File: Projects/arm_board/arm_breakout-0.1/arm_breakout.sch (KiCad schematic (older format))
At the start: 4 parts, among them P1 CONN_3X2, U1 2534-6002UB_34-pin_header, U2 Teensy3.1, U3 MCP2561

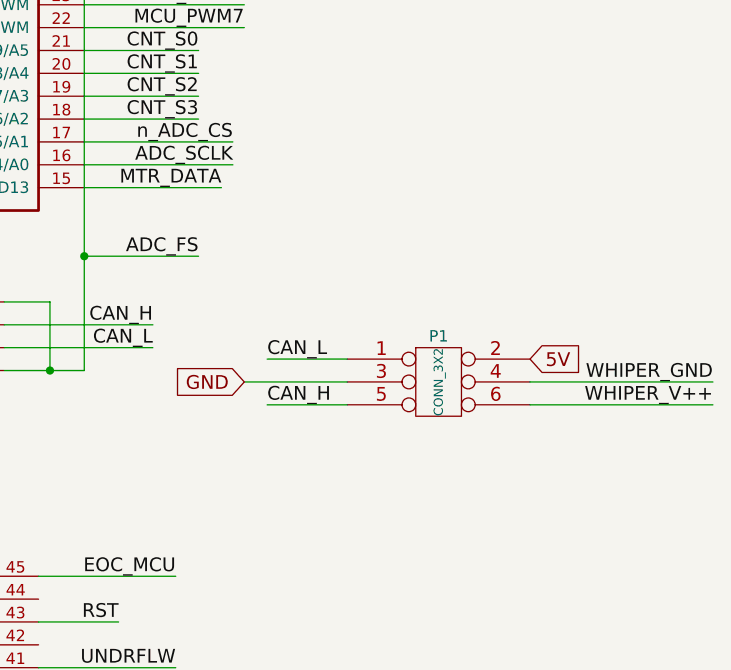
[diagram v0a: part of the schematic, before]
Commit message: Arm Breakout: Finish schematic, assign footprints
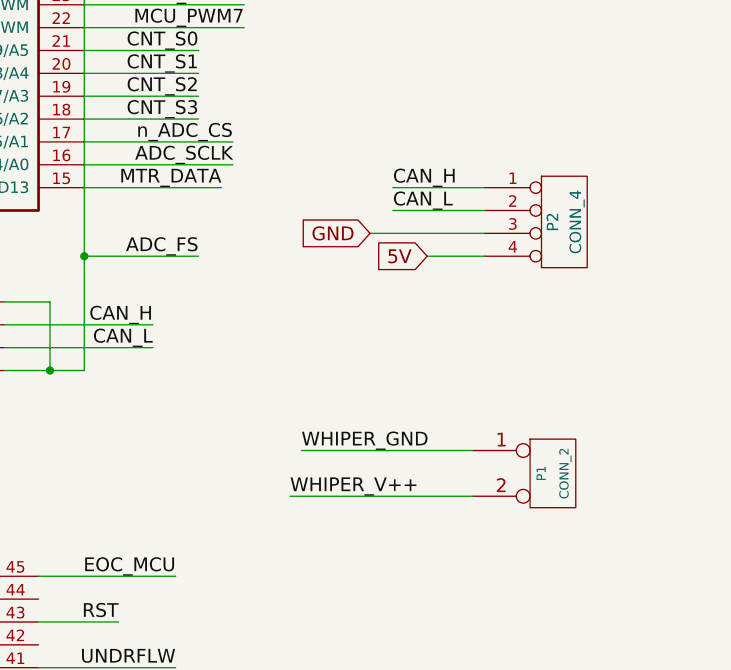
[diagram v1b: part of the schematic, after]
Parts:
- removed P1: CONN_3X2, symbol CONN_3X2
- added P1: CONN_2, ArmFootprints:2-pin-connector, symbol CONN_2
- added P2: CONN_4, ArmFootprints:4-pin_connector, symbol CONN_4
- U1: footprint (none) -> ArmFootprints:34-pin_2534-6002UB
- U2: footprint (none) -> ArmFootprints:Teensy3.1
- U3: footprint (none) -> ArmFootprints:MCP2562
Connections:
- net 5V: now also P2.4 (P4)
- net CAN_H: now also P2.1 (P1)
- net CAN_L: now also P2.2 (P2)
- net GND: now also P2.3 (P3)
- net WHIPER_GND: now also P1.1 (P1)
- net WHIPER_V++: now also P1.2 (PM)
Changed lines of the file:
@@
 F 0 "U3" H 4950 4500 60  0000 L CNN
 F 1 "MCP2561" H 4950 4400 60  0000 L CNN
-F 2 "" H 4750 4250 60  0000 C CNN
+F 2 "ArmFootprints:MCP2562" H 4750 4250 60  0001 C CNN
 F 3 "" H 4750 4250 60  0000 C CNN
 	1    5300 4150
@@
 F 0 "U1" H 2100 2200 60  0000 C CNN
 F 1 "2534-6002UB_34-pin_header" V 2100 3100 60  0000 C CNN
-F 2 "" H 2100 3250 60  0000 C CNN
+F 2 "ArmFootprints:34-pin_2534-6002UB" H 2100 3250 60  0001 C CNN
 F 3 "" H 2100 3250 60  0000 C CNN
 	1    2100 3250
@@
 F 0 "U2" H 4600 2500 60  0000 L CNN
 F 1 "Teensy3.1" H 4600 2400 60  0000 L CNN
-F 2 "" H 4400 2250 60  0000 C CNN
+F 2 "ArmFootprints:Teensy3.1" H 4400 2250 60  0001 C CNN
 F 3 "" H 4400 2250 60  0000 C CNN
 	3    4400 2250
@@
 F 0 "U2" H 4800 5200 60  0000 L CNN
 F 1 "Teensy3.1" H 4800 5100 60  0000 L CNN
-F 2 "" H 4600 4950 60  0000 C CNN
+F 2 "ArmFootprints:Teensy3.1" H 4600 4950 60  0001 C CNN
 F 3 "" H 4600 4950 60  0000 C CNN
 	2    4600 4950
@@
 Text GLabel 3900 2250 0    60   Input ~ 0
 GND
-$Comp
-L CONN_3X2 P1
-U 1 1 57225D6F
-P 7750 4450
-F 0 "P1" H 7750 4700 50  0000 C CNN
-F 1 "CONN_3X2" V 7750 4500 40  0000 C CNN
-F 2 "" H 7750 4450 60  0000 C CNN
-F 3 "" H 7750 4450 60  0000 C CNN
-	1    7750 4450
-	1    0    0    -1
-$EndComp
-Text GLabel 8150 4300 2    60   Input ~ 0
-5V
-Text GLabel 6900 4400 0    60   Input ~ 0
-GND
-Text Label 8950 4400 2    60   ~ 0
+Text Label 7150 4700 0    60   ~ 0
 WHIPER_GND
-Text Label 8950 4500 2    60   ~ 0
+Text Label 7100 4900 0    60   ~ 0
 WHIPER_V++
-Text Label 7000 4500 0    60   ~ 0
-CAN_H
 Wire Wire Line
 	1300 2550 1800 2550
@@
 Wire Wire Line
 	6200 4350 5850 4350
-Wire Wire Line
-	8950 4400 8150 4400
-Wire Wire Line
-	8950 4500 8150 4500
-Wire Wire Line
-	7000 4500 7350 4500
-Text Label 7000 4300 0    60   ~ 0
-CAN_L
-Wire Wire Line
-	7000 4300 7350 4300
-Wire Wire Line
-	6900 4400 7350 4400
 Text Label 6500 4250 2    60   ~ 0
 CAN_L
@@
 	6050 4050 6050 4350
 Connection ~ 6050 4350
+$Comp
+L CONN_4 P2
+U 1 1 57226EBC
+P 8300 3700
+F 0 "P2" V 8250 3700 50  0000 C CNN
+F 1 "CONN_4" V 8350 3700 50  0000 C CNN
+F 2 "ArmFootprints:4-pin_connector" H 8300 3700 60  0001 C CNN
+F 3 "" H 8300 3700 60  0000 C CNN
+	1    8300 3700
+	1    0    0    -1
+$EndComp
+Text Label 7550 3550 0    60   ~ 0
+CAN_H
+Text Label 7550 3650 0    60   ~ 0
+CAN_L
+Text GLabel 7450 3750 0    60   Input ~ 0
+GND
+Text GLabel 7700 3850 0    60   Input ~ 0
+5V
+Wire Wire Line
+	7700 3850 7950 3850
+Wire Wire Line
+	7450 3750 7950 3750
+Wire Wire Line
+	7550 3650 7950 3650
+Wire Wire Line
+	7950 3550 7550 3550
+$Comp
+L CONN_2 P1
+U 1 1 57227184
+P 8250 4800
+F 0 "P1" V 8200 4800 40  0000 C CNN
+F 1 "CONN_2" V 8300 4800 40  0000 C CNN
+F 2 "ArmFootprints:2-pin-connector" H 8250 4800 60  0001 C CNN
+F 3 "" H 8250 4800 60  0000 C CNN
+	1    8250 4800
+	1    0    0    -1
+$EndComp
+Wire Wire Line
+	7900 4900 7100 4900
+Wire Wire Line
+	7150 4700 7900 4700
 $EndSCHEMATC

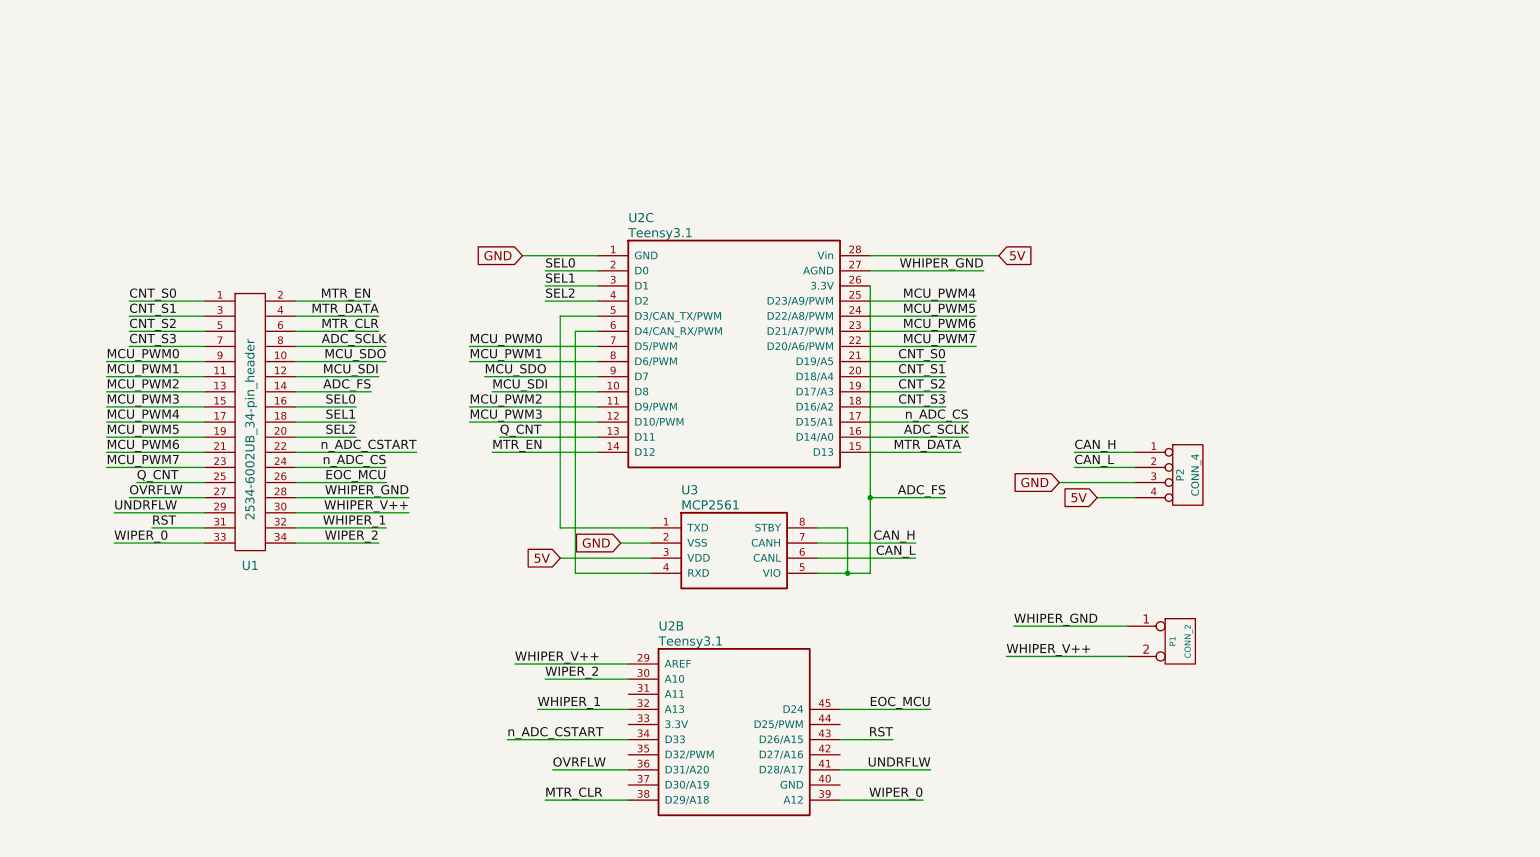
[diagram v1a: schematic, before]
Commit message: Arm Breakout: made pcb layout
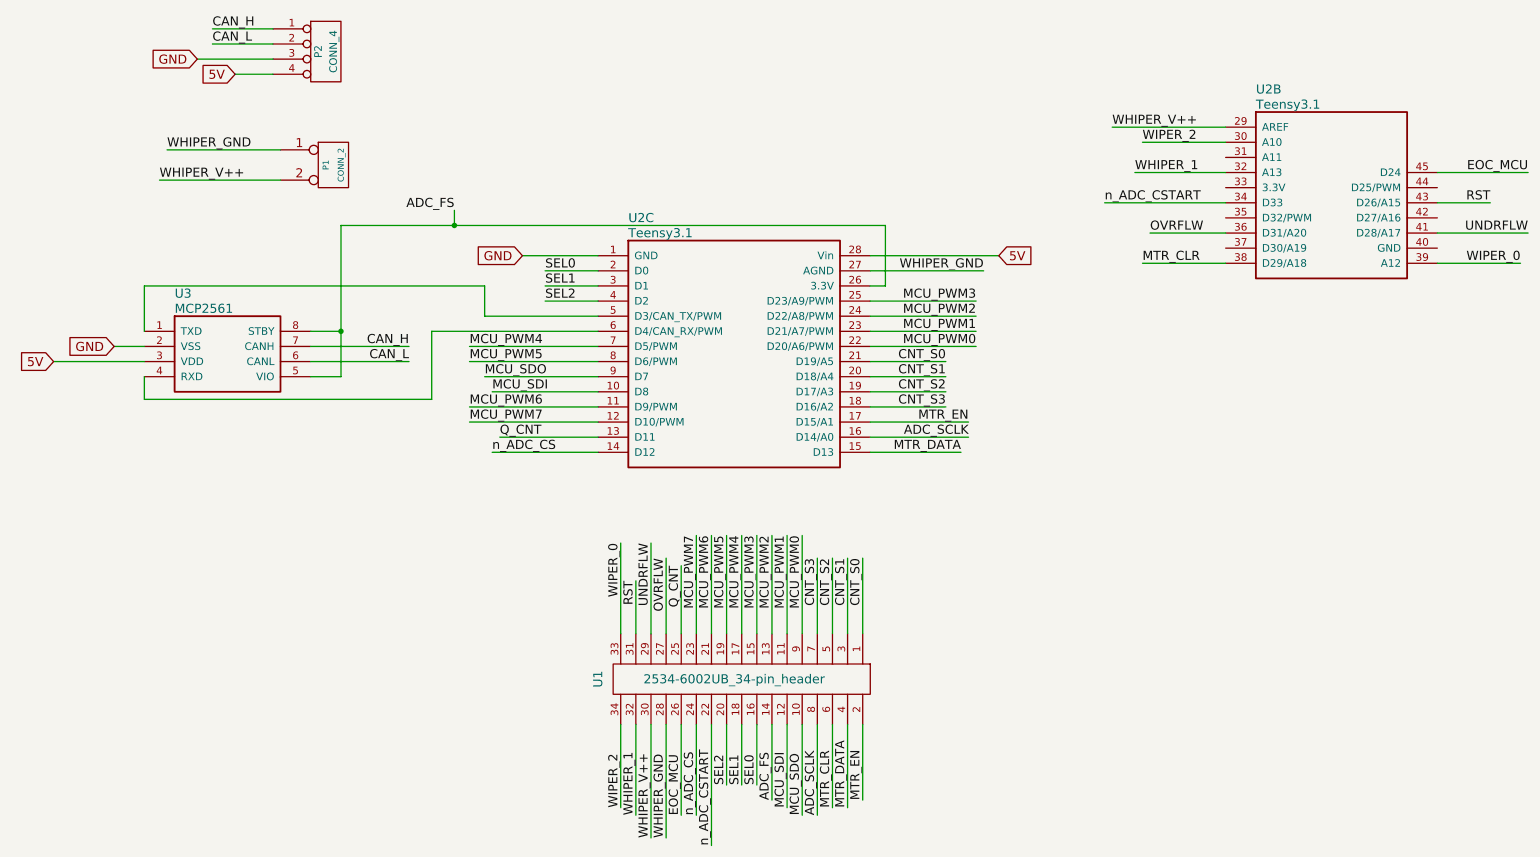
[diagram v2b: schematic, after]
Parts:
- U3: footprint ArmFootprints:MCP2562 -> ArmFootprints:MCP2562_dip
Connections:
- net MCU_PWM0: now also U2.22 (D20/A6/PWM); no longer U2.7 (D5/PWM)
- net MCU_PWM1: now also U2.23 (D21/A7/PWM); no longer U2.8 (D6/PWM)
- net MCU_PWM2: now also U2.24 (D22/A8/PWM); no longer U2.11 (D9/PWM)
- net MCU_PWM3: now also U2.25 (D23/A9/PWM); no longer U2.12 (D10/PWM)
- net MCU_PWM4: now also U2.7 (D5/PWM); no longer U2.25 (D23/A9/PWM)
- net MCU_PWM5: now also U2.8 (D6/PWM); no longer U2.24 (D22/A8/PWM)
- net MCU_PWM6: now also U2.11 (D9/PWM); no longer U2.23 (D21/A7/PWM)
- net MCU_PWM7: now also U2.12 (D10/PWM); no longer U2.22 (D20/A6/PWM)
- net MTR_EN: now also U2.17 (D15/A1); no longer U2.14 (D12)
- net n_ADC_CS: now also U2.14 (D12); no longer U2.17 (D15/A1)
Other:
- moved on the sheet: P1, P2, U1, U2B, U3

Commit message: Arm Breakout: increased 34 pin header pad size
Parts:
- U1: footprint ArmFootprints:34-pin_2534-6002UB -> ArmFootprints:34-pin_2534-6002UB_WIDE
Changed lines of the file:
@@
 F 0 "U1" H 5450 4000 60  0000 C CNN
 F 1 "2534-6002UB_34-pin_header" V 5450 4900 60  0000 C CNN
-F 2 "ArmFootprints:34-pin_2534-6002UB" H 5450 5050 60  0001 C CNN
+F 2 "ArmFootprints:34-pin_2534-6002UB_WIDE" H 5450 5050 60  0001 C CNN
 F 3 "" H 5450 5050 60  0000 C CNN
 	1    5450 5050
